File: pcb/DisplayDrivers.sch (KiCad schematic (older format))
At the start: 0 parts

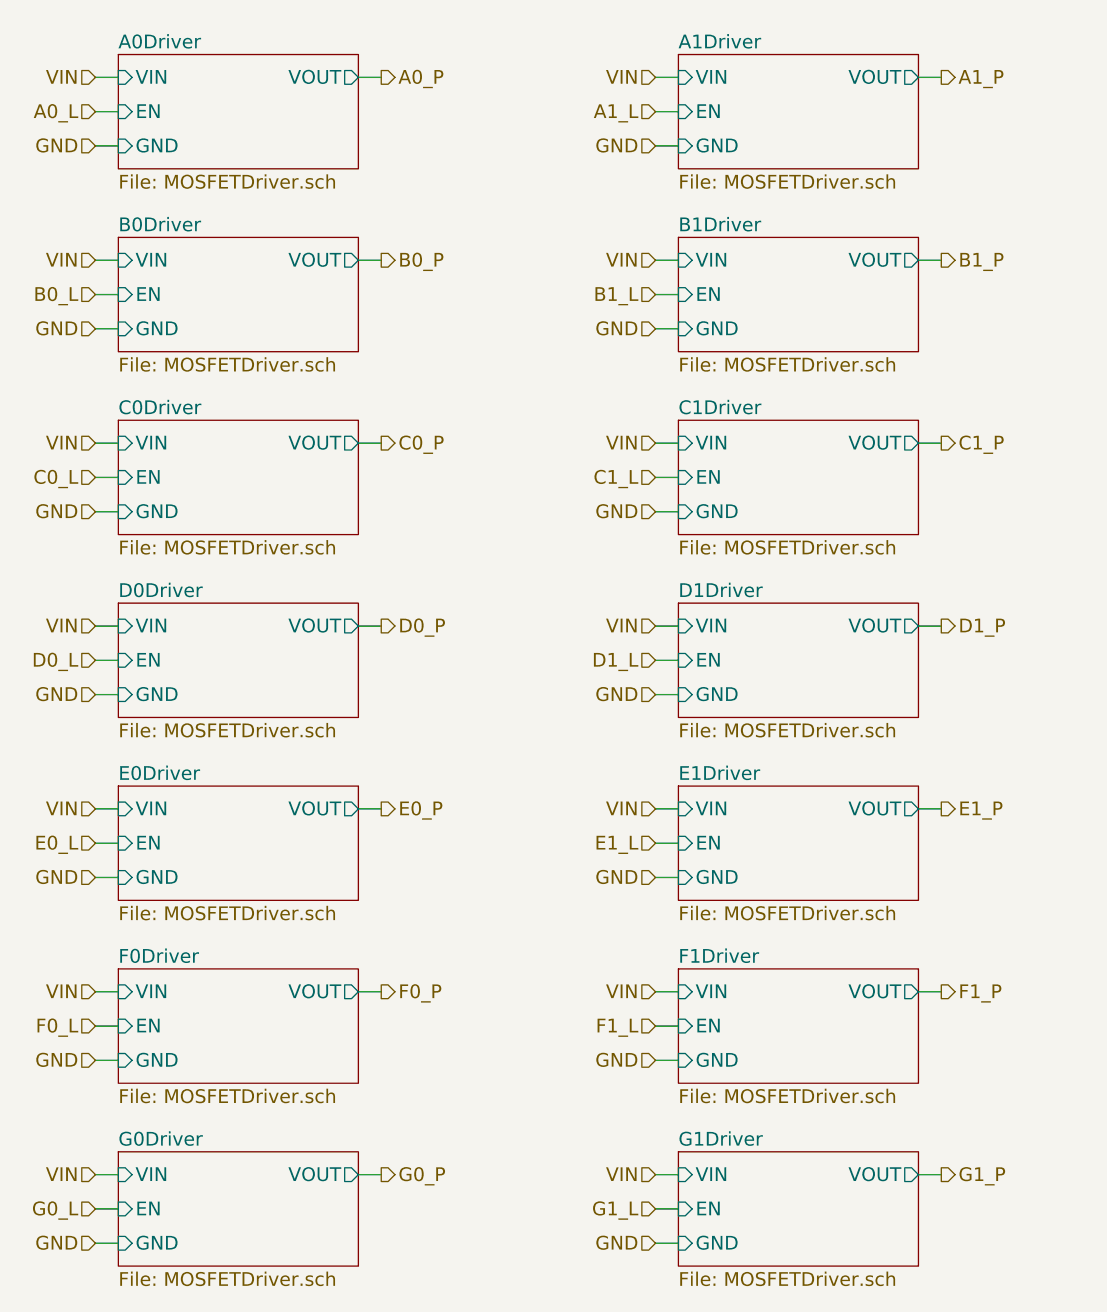
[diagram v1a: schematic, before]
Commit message: Current-limiting resistors on the display segments
Missed these on the first pass because I copied the drivers from the
RYG tower but forgot that they have integrated resistors.
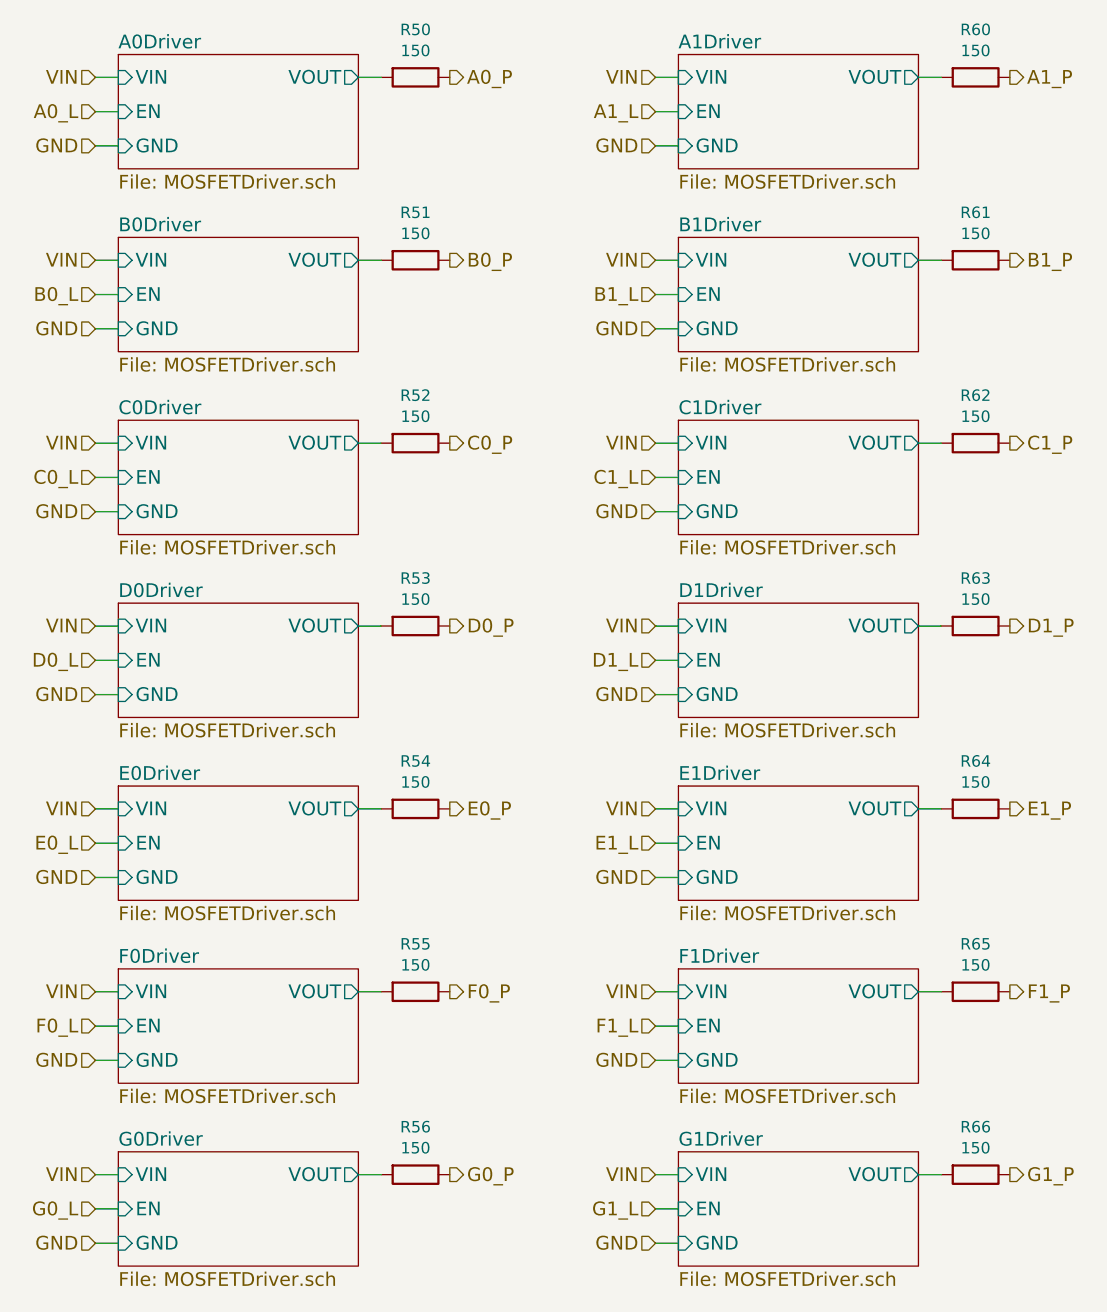
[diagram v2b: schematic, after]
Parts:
- added R50, R51, R52, R53, R54, R55, R56, R60, R61, R62, R63, R64, R65, R66: 150, Discret:R3, symbol R
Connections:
- net A0_P: now also R50.1
- net A1_P: now also R60.1
- net B0_P: now also R51.1
- net B1_P: now also R61.1
- net C0_P: now also R52.1
- net C1_P: now also R62.1
- net D0_P: now also R53.1
- net D1_P: now also R63.1
- net E0_P: now also R54.1
- net E1_P: now also R64.1
- net F0_P: now also R55.1
- net F1_P: now also R65.1
- net G0_P: now also R56.1
- net G1_P: now also R66.1
- new net A0Driver/VOUT: R50.2
- new net A1Driver/VOUT: R60.2
- new net B0Driver/VOUT: R51.2
- new net B1Driver/VOUT: R61.2
- new net C0Driver/VOUT: R52.2
- new net C1Driver/VOUT: R62.2
- new net D0Driver/VOUT: R53.2
- new net D1Driver/VOUT: R63.2
- new net E0Driver/VOUT: R54.2
- new net E1Driver/VOUT: R64.2
- new net F0Driver/VOUT: R55.2
- new net F1Driver/VOUT: R65.2
- new net G0Driver/VOUT: R56.2
- new net G1Driver/VOUT: R66.2
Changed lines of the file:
@@
 Text HLabel 1750 6350 0    60   Input ~ 0
 G0_L
-Text HLabel 3000 1400 2    60   Output ~ 0
+Text HLabel 3300 1400 2    60   Output ~ 0
 A0_P
-Text HLabel 3000 2200 2    60   Output ~ 0
+Text HLabel 3300 2200 2    60   Output ~ 0
 B0_P
-Text HLabel 3000 3000 2    60   Output ~ 0
+Text HLabel 3300 3000 2    60   Output ~ 0
 C0_P
-Text HLabel 3000 3800 2    60   Output ~ 0
+Text HLabel 3300 3800 2    60   Output ~ 0
 D0_P
-Text HLabel 3000 4600 2    60   Output ~ 0
+Text HLabel 3300 4600 2    60   Output ~ 0
 E0_P
-Text HLabel 3000 5400 2    60   Output ~ 0
+Text HLabel 3300 5400 2    60   Output ~ 0
 F0_P
-Text HLabel 3000 6200 2    60   Output ~ 0
+Text HLabel 3300 6200 2    60   Output ~ 0
 G0_P
 $Sheet
@@
 Text HLabel 4200 6350 0    60   Input ~ 0
 G1_L
-Text HLabel 5450 1400 2    60   Output ~ 0
+Text HLabel 5750 1400 2    60   Output ~ 0
 A1_P
-Text HLabel 5450 2200 2    60   Output ~ 0
+Text HLabel 5750 2200 2    60   Output ~ 0
 B1_P
-Text HLabel 5450 3000 2    60   Output ~ 0
+Text HLabel 5750 3000 2    60   Output ~ 0
 C1_P
-Text HLabel 5450 3800 2    60   Output ~ 0
+Text HLabel 5750 3800 2    60   Output ~ 0
 D1_P
-Text HLabel 5450 4600 2    60   Output ~ 0
+Text HLabel 5750 4600 2    60   Output ~ 0
 E1_P
-Text HLabel 5450 5400 2    60   Output ~ 0
+Text HLabel 5750 5400 2    60   Output ~ 0
 F1_P
-Text HLabel 5450 6200 2    60   Output ~ 0
+Text HLabel 5750 6200 2    60   Output ~ 0
 G1_P
+$Comp
+L R R50
+U 1 1 56CA080D
+P 3150 1400
+F 0 "R50" V 2942 1400 50  0000 C CNN
+F 1 "150" V 3034 1400 50  0000 C CNN
+F 2 "Discret:R3" V 3080 1400 50  0001 C CNN
+F 3 "" H 3150 1400 50  0000 C CNN
+	1    3150 1400
+	0    1    1    0
+$EndComp
+$Comp
+L R R51
+U 1 1 56CA15A3
+P 3150 2200
+F 0 "R51" V 2942 2200 50  0000 C CNN
+F 1 "150" V 3034 2200 50  0000 C CNN
+F 2 "Discret:R3" V 3080 2200 50  0001 C CNN
+F 3 "" H 3150 2200 50  0000 C CNN
+	1    3150 2200
+	0    1    1    0
+$EndComp
+$Comp
+L R R52
+U 1 1 56CA1C7E
+P 3150 3000
+F 0 "R52" V 2942 3000 50  0000 C CNN
+F 1 "150" V 3034 3000 50  0000 C CNN
+F 2 "Discret:R3" V 3080 3000 50  0001 C CNN
+F 3 "" H 3150 3000 50  0000 C CNN
+	1    3150 3000
+	0    1    1    0
+$EndComp
+$Comp
+L R R53
+U 1 1 56CA2213
+P 3150 3800
+F 0 "R53" V 2942 3800 50  0000 C CNN
+F 1 "150" V 3034 3800 50  0000 C CNN
+F 2 "Discret:R3" V 3080 3800 50  0001 C CNN
+F 3 "" H 3150 3800 50  0000 C CNN
+	1    3150 3800
+	0    1    1    0
+$EndComp
+$Comp
+L R R54
+U 1 1 56CA2B0B
+P 3150 4600
+F 0 "R54" V 2942 4600 50  0000 C CNN
+F 1 "150" V 3034 4600 50  0000 C CNN
+F 2 "Discret:R3" V 3080 4600 50  0001 C CNN
+F 3 "" H 3150 4600 50  0000 C CNN
+	1    3150 4600
+	0    1    1    0
+$EndComp
+$Comp
+L R R55
+U 1 1 56CA2F5E
+P 3150 5400
+F 0 "R55" V 2942 5400 50  0000 C CNN
+F 1 "150" V 3034 5400 50  0000 C CNN
+F 2 "Discret:R3" V 3080 5400 50  0001 C CNN
+F 3 "" H 3150 5400 50  0000 C CNN
+	1    3150 5400
+	0    1    1    0
+$EndComp
+$Comp
+L R R56
+U 1 1 56CA35C0
+P 3150 6200
+F 0 "R56" V 2942 6200 50  0000 C CNN
+F 1 "150" V 3034 6200 50  0000 C CNN
+F 2 "Discret:R3" V 3080 6200 50  0001 C CNN
+F 3 "" H 3150 6200 50  0000 C CNN
+	1    3150 6200
+	0    1    1    0
+$EndComp
+$Comp
+L R R60
+U 1 1 56CA4259
+P 5600 1400
+F 0 "R60" V 5392 1400 50  0000 C CNN
+F 1 "150" V 5484 1400 50  0000 C CNN
+F 2 "Discret:R3" V 5530 1400 50  0001 C CNN
+F 3 "" H 5600 1400 50  0000 C CNN
+	1    5600 1400
+	0    1    1    0
+$EndComp
+$Comp
+L R R61
+U 1 1 56CA46E5
+P 5600 2200
+F 0 "R61" V 5392 2200 50  0000 C CNN
+F 1 "150" V 5484 2200 50  0000 C CNN
+F 2 "Discret:R3" V 5530 2200 50  0001 C CNN
+F 3 "" H 5600 2200 50  0000 C CNN
+	1    5600 2200
+	0    1    1    0
+$EndComp
+$Comp
+L R R62
+U 1 1 56CA4E36
+P 5600 3000
+F 0 "R62" V 5392 3000 50  0000 C CNN
+F 1 "150" V 5484 3000 50  0000 C CNN
+F 2 "Discret:R3" V 5530 3000 50  0001 C CNN
+F 3 "" H 5600 3000 50  0000 C CNN
+	1    5600 3000
+	0    1    1    0
+$EndComp
+$Comp
+L R R63
+U 1 1 56CA52B4
+P 5600 3800
+F 0 "R63" V 5392 3800 50  0000 C CNN
+F 1 "150" V 5484 3800 50  0000 C CNN
+F 2 "Discret:R3" V 5530 3800 50  0001 C CNN
+F 3 "" H 5600 3800 50  0000 C CNN
+	1    5600 3800
+	0    1    1    0
+$EndComp
+$Comp
+L R R64
+U 1 1 56CA5A0F
+P 5600 4600
+F 0 "R64" V 5392 4600 50  0000 C CNN
+F 1 "150" V 5484 4600 50  0000 C CNN
+F 2 "Discret:R3" V 5530 4600 50  0001 C CNN
+F 3 "" H 5600 4600 50  0000 C CNN
+	1    5600 4600
+	0    1    1    0
+$EndComp
+$Comp
+L R R65
+U 1 1 56CA6240
+P 5600 5400
+F 0 "R65" V 5392 5400 50  0000 C CNN
+F 1 "150" V 5484 5400 50  0000 C CNN
+F 2 "Discret:R3" V 5530 5400 50  0001 C CNN
+F 3 "" H 5600 5400 50  0000 C CNN
+	1    5600 5400
+	0    1    1    0
+$EndComp
+$Comp
+L R R66
+U 1 1 56CA69AD
+P 5600 6200
+F 0 "R66" V 5392 6200 50  0000 C CNN
+F 1 "150" V 5484 6200 50  0000 C CNN
+F 2 "Discret:R3" V 5530 6200 50  0001 C CNN
+F 3 "" H 5600 6200 50  0000 C CNN
+	1    5600 6200
+	0    1    1    0
+$EndComp
 $EndSCHEMATC
